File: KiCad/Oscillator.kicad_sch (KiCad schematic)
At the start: 36 parts, among them Q1 NPN, Q2 PNP, Q3 NPN, Q4 PNP, U4 40106, U5 TL074

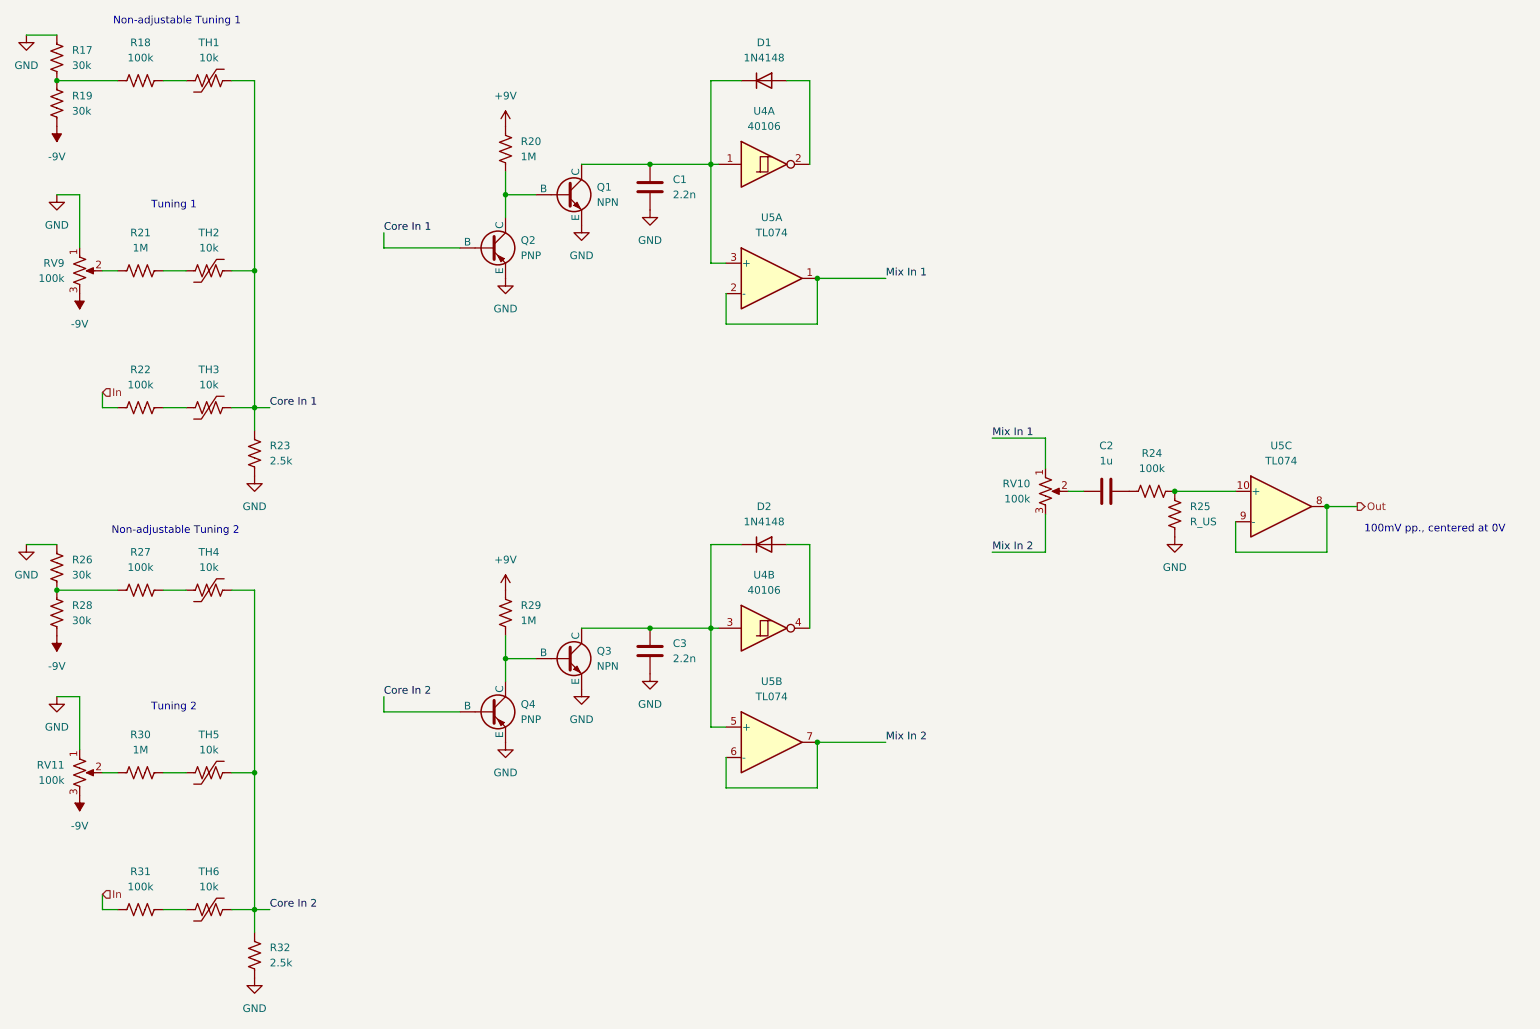
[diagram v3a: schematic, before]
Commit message: added power switch, decoupling caps, and unused IC pins
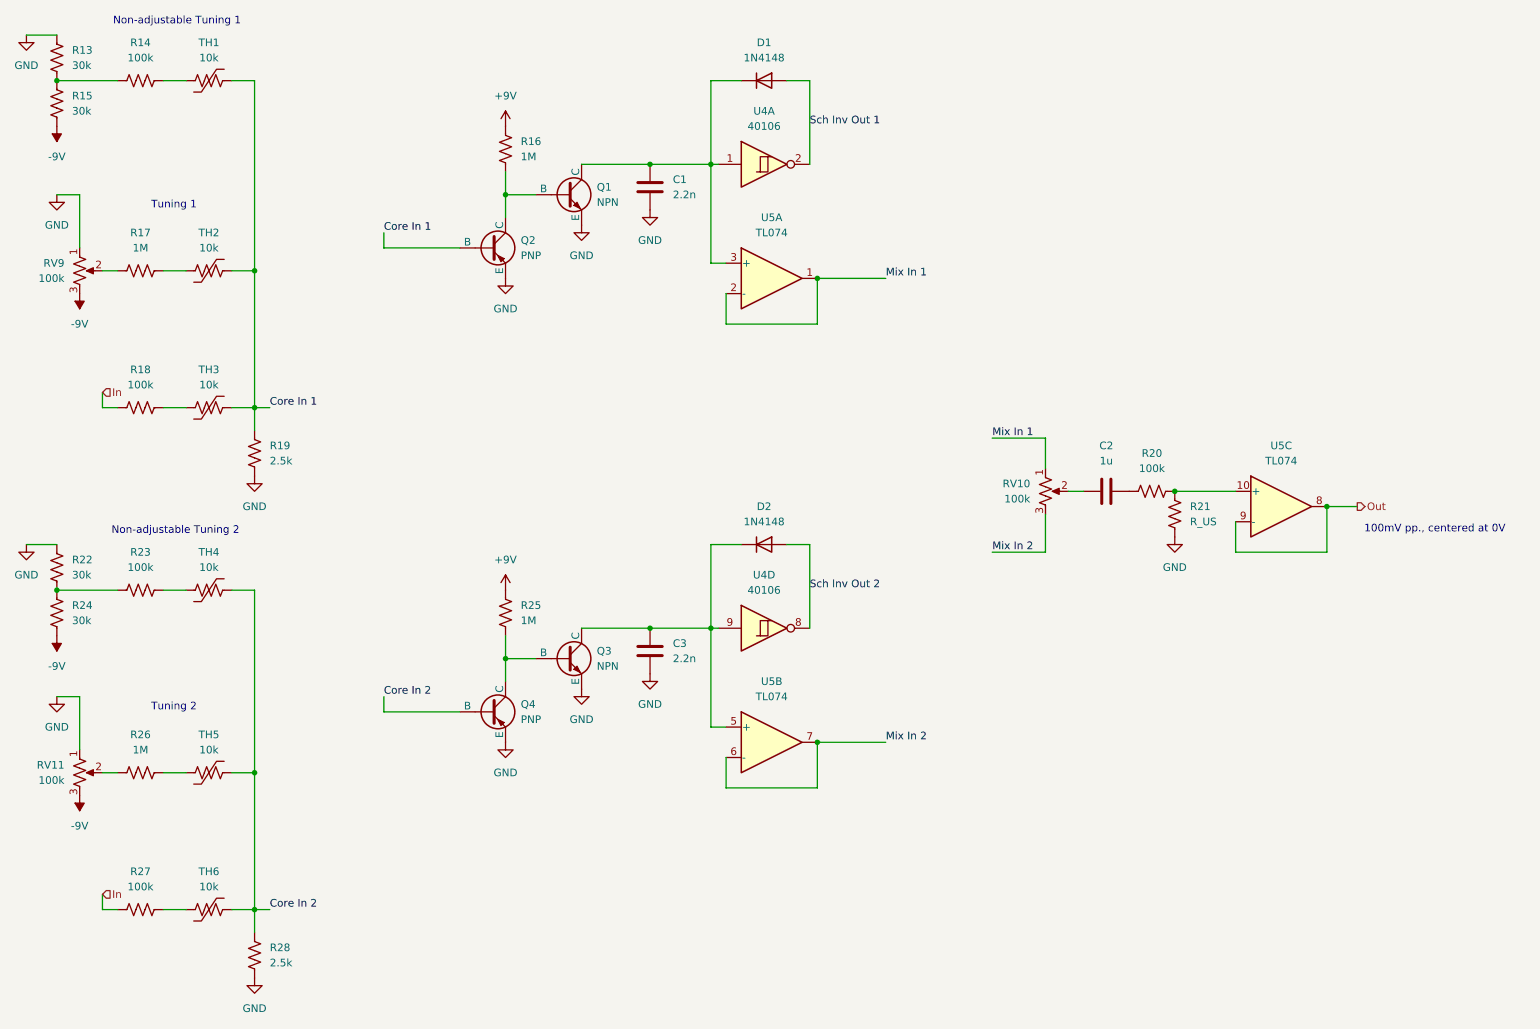
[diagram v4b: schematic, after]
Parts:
- RV10, RV11, RV9: footprint Potentiometer 51CAD_E24_A20L:POT_51CAD_12P5X13P25_BRN -> Potentiometer 100k PTV09A-2020F-B104:Potentiometer 100k PTV09A-2020F-B104
- renumbered R17 to R13, R18 to R14, R19 to R15, R20 to R16, R21 to R17, R22 to R18, R23 to R19, R24 to R20, R25 to R21, R26 to R22, R27 to R23, R28 to R24, R29 to R25, R30 to R26, R31 to R27, R32 to R28
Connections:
- net at C3.1, D2.1 (K), Q3.1 (C)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: now also U4.9; no longer U4.3
- net Sch Inv Out 2: now reaches D2.2 (A)
- net Sch Inv Out 2: now also U4.8; no longer U4.4
- net Sch Inv Out 1: now reaches D1.2 (A), U4.2
